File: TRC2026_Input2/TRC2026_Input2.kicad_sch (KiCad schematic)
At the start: 25 parts, among them J1 Conn_01x06_Pin, J2 Conn_01x06_Pin, J3 Conn_01x05_Pin, J4 Conn_01x05_Pin, J5 Conn_01x05_Pin, J6 Conn_01x05_Pin, SW1 SW_Push, SW2 SW_Push, SW3 SW_Push, SW4 SW_Push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

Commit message: kairozukousin
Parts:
- added R1, R2, R3, R4: 3.3k, symbol Device:R
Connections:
- net GND: now also R1.1, R2.2, R3.2, R4.1
- net GP2: now also R1.2
- net GP3: now also R4.2
- net GP4: now also R2.1
- net GP5: now also R3.1

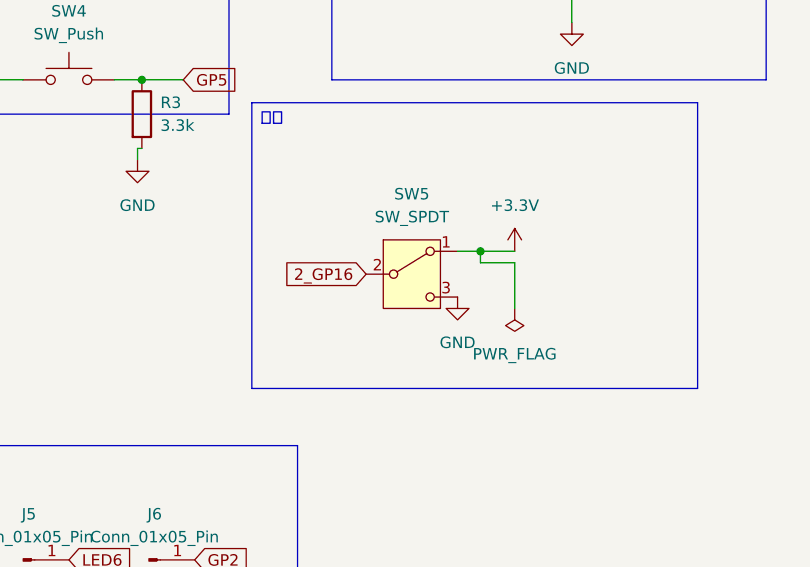
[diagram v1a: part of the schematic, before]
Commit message: プルダウン抵抗とフットプリントを修正しました
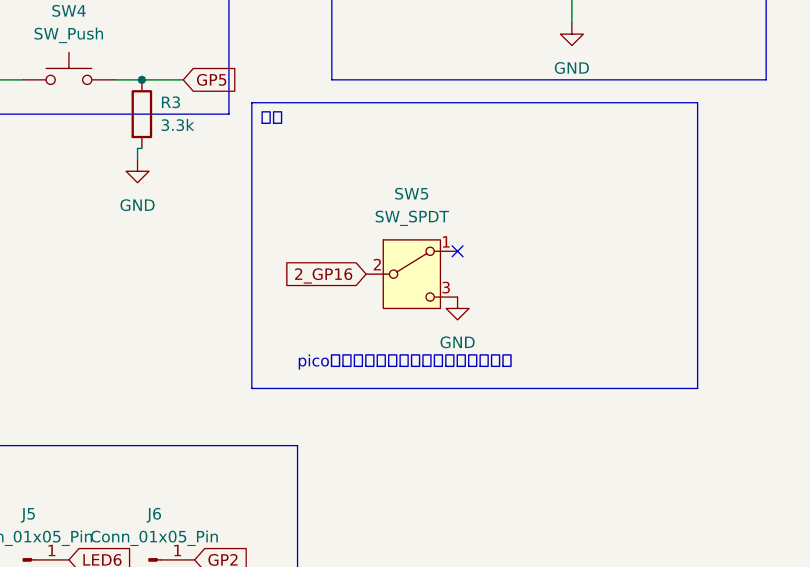
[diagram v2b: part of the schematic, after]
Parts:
- R1, R2, R3, R4: footprint (none) -> Resistor_THT:R_Axial_DIN0207_L6.3mm_D2.5mm_P10.16mm_Horizontal
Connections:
- net +3.3V: no longer SW5.1 (A)
- no-connect marks 6 -> 7
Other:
- note added: "picoの内蔵プルアップ抵抗を入れること"
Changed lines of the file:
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@@
 	(generator_version "9.0")
 	(paper "A4")
+	(text "picoの内蔵プルアップ抵抗を入れること"
+		(exclude_from_sim no)
+		(at 98.298 106.426 0)
+		(effects
+			(font
+				(size 1.27 1.27)
+			)
+		)
+	)
 	(text_box "電源チェック"
 		(exclude_from_sim no)
@@
 	)
 	(junction
-		(at 106.68 93.98)
-		(diameter 0)
-		(color 0 0 0 0)
-	)
-	(junction
 		(at 116.84 64.77)
 		(diameter 0)
@@
 	)
 	(no_connect
+		(at 104.14 93.98)
+	)
+	(no_connect
 		(at 125.73 62.23)
 	)
@@
 	(wire
 		(pts
-			(xy 110.49 93.98) (xy 106.68 93.98)
-		)
-		(stroke
-			(width 0)
-			(type default)
-		)
-	)
-	(wire
-		(pts
 			(xy 185.42 92.71) (xy 185.42 96.52)
 		)
@@
 	(wire
 		(pts
-			(xy 106.68 95.25) (xy 106.68 93.98)
-		)
-		(stroke
-			(width 0)
-			(type default)
-		)
-	)
-	(wire
-		(pts
 			(xy 34.29 121.92) (xy 34.29 130.81)
 		)
@@
 	(wire
 		(pts
-			(xy 110.49 100.33) (xy 110.49 95.25)
-		)
-		(stroke
-			(width 0)
-			(type default)
-		)
-	)
-	(wire
-		(pts
 			(xy 68.58 82.55) (xy 69.0633 82.55)
 		)
@@
 	(wire
 		(pts
-			(xy 106.68 93.98) (xy 104.14 93.98)
-		)
-		(stroke
-			(width 0)
-			(type default)
-		)
-	)
-	(wire
-		(pts
-			(xy 110.49 95.25) (xy 106.68 95.25)
-		)
-		(stroke
-			(width 0)
-			(type default)
-		)
-	)
-	(wire
-		(pts
 			(xy 41.91 74.93) (xy 39.37 74.93)
 		)
@@
 			)
 		)
-		(property "Footprint" ""
+		(property "Footprint" "Resistor_THT:R_Axial_DIN0207_L6.3mm_D2.5mm_P10.16mm_Horizontal"
 			(at 67.2853 78.74 90)
 			(effects
@@
 	(symbol
 		(lib_id "power:+3.3V")
-		(at 110.49 93.98 0)
-		(unit 1)
-		(exclude_from_sim no)
-		(in_bom yes)
-		(on_board yes)
-		(dnp no)
-		(fields_autoplaced yes)
-		(property "Reference" "#PWR019"
-			(at 110.49 97.79 0)
-			(effects
-				(font
-					(size 1.27 1.27)
-				)
-				(hide yes)
-			)
-		)
-		(property "Value" "+3.3V"
-			(at 110.49 88.9 0)
-			(effects
-				(font
-					(size 1.27 1.27)
-				)
-			)
-		)
-		(property "Footprint" ""
-			(at 110.49 93.98 0)
-			(effects
-				(font
-					(size 1.27 1.27)
-				)
-				(hide yes)
-			)
-		)
-		(property "Datasheet" ""
-			(at 110.49 93.98 0)
-			(effects
-				(font
-					(size 1.27 1.27)
-				)
-				(hide yes)
-			)
-		)
-		(property "Description" "Power symbol creates a global label with name \"+3.3V\""
-			(at 110.49 93.98 0)
-			(effects
-				(font
-					(size 1.27 1.27)
-				)
-				(hide yes)
-			)
-		)
-		(pin "1"
-		)
-		(instances
-			(project "TRC2026_Input2"
-				(path "/b8b83729-b4aa-4a20-8577-ec48fda0bc33"
-					(reference "#PWR019")
-					(unit 1)
-				)
-			)
-		)
-	)
-	(symbol
-		(lib_id "power:+3.3V")
 		(at 49.53 74.93 0)
 		(unit 1)
@@
 			)
 		)
-		(property "Footprint" ""
+		(property "Footprint" "Resistor_THT:R_Axial_DIN0207_L6.3mm_D2.5mm_P10.16mm_Horizontal"
 			(at 37.592 58.42 90)
 			(effects
@@
 	)
 	(symbol
-		(lib_id "power:PWR_FLAG")
-		(at 110.49 100.33 180)
-		(unit 1)
-		(exclude_from_sim no)
-		(in_bom yes)
-		(on_board yes)
-		(dnp no)
-		(fields_autoplaced yes)
-		(property "Reference" "#FLG05"
-			(at 110.49 102.235 0)
-			(effects
-				(font
-					(size 1.27 1.27)
-				)
-				(hide yes)
-			)
-		)
-		(property "Value" "PWR_FLAG"
-			(at 110.49 105.41 0)
-			(effects
-				(font
-					(size 1.27 1.27)
-				)
-			)
-		)
-		(property "Footprint" ""
-			(at 110.49 100.33 0)
-			(effects
-				(font
-					(size 1.27 1.27)
-				)
-				(hide yes)
-			)
-		)
-		(property "Datasheet" "~"
-			(at 110.49 100.33 0)
-			(effects
-				(font
-					(size 1.27 1.27)
-				)
-				(hide yes)
-			)
-		)
-		(property "Description" "Special symbol for telling ERC where power comes from"
-			(at 110.49 100.33 0)
-			(effects
-				(font
-					(size 1.27 1.27)
-				)
-				(hide yes)
-			)
-		)
-		(pin "1"
-		)
-		(instances
-			(project "TRC2026_Input2"
-				(path "/b8b83729-b4aa-4a20-8577-ec48fda0bc33"
-					(reference "#FLG05")
-					(unit 1)
-				)
-			)
-		)
-	)
-	(symbol
 		(lib_id "Switch:SW_SPDT")
 		(at 99.06 96.52 0)
@@
 			)
 		)
-		(property "Footprint" ""
+		(property "Footprint" "Resistor_THT:R_Axial_DIN0207_L6.3mm_D2.5mm_P10.16mm_Horizontal"
 			(at 68.072 58.42 90)
 			(effects
@@
 			)
 		)
-		(property "Footprint" ""
+		(property "Footprint" "Resistor_THT:R_Axial_DIN0207_L6.3mm_D2.5mm_P10.16mm_Horizontal"
 			(at 37.592 78.74 90)
 			(effects
